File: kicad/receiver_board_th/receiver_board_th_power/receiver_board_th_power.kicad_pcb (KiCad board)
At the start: 2 copper layers, 31 x 63 mm, 12 parts, among them J1 B2B 1, J2 B2B 2, J3 Motor 1, J4 Motor 2, J5 Battery Mon, U1 ESP32-C3-SuperMini, U2 Dual H Bridge

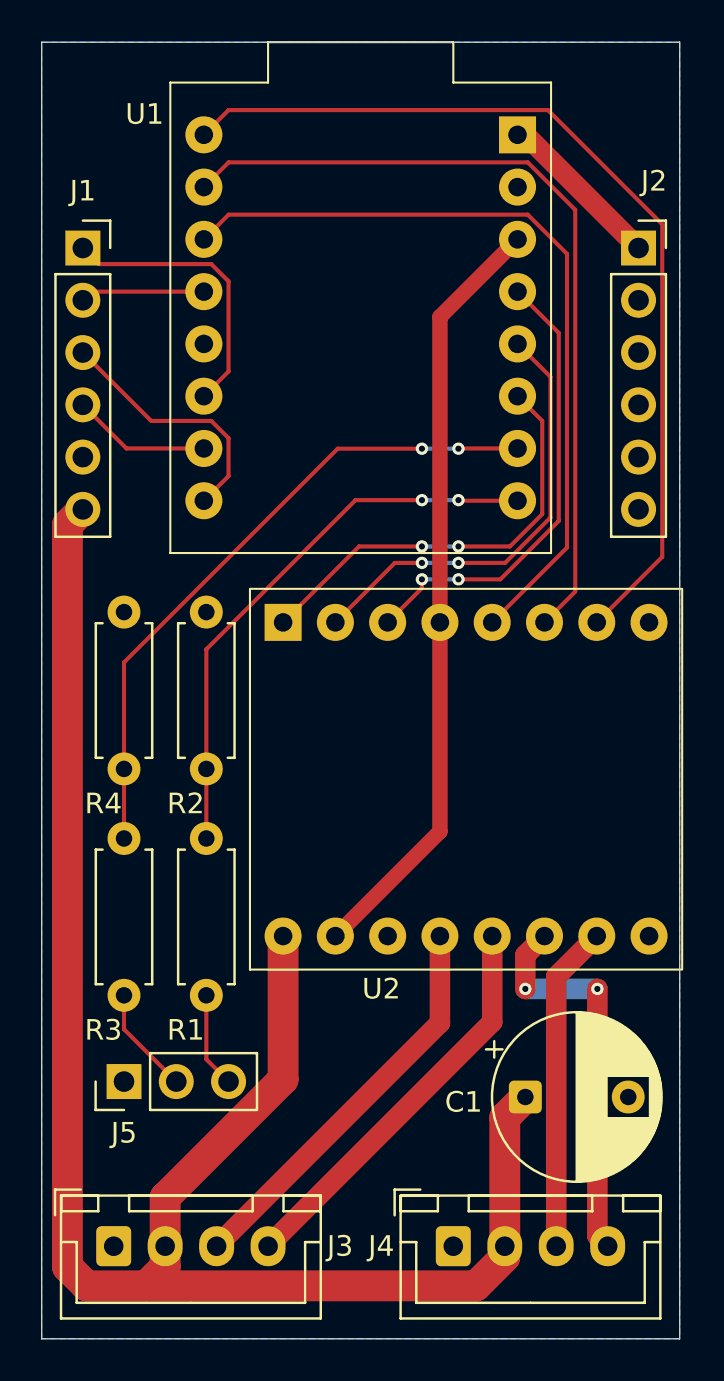
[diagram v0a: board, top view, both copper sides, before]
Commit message: Add M2 mounting holes to receiver power board
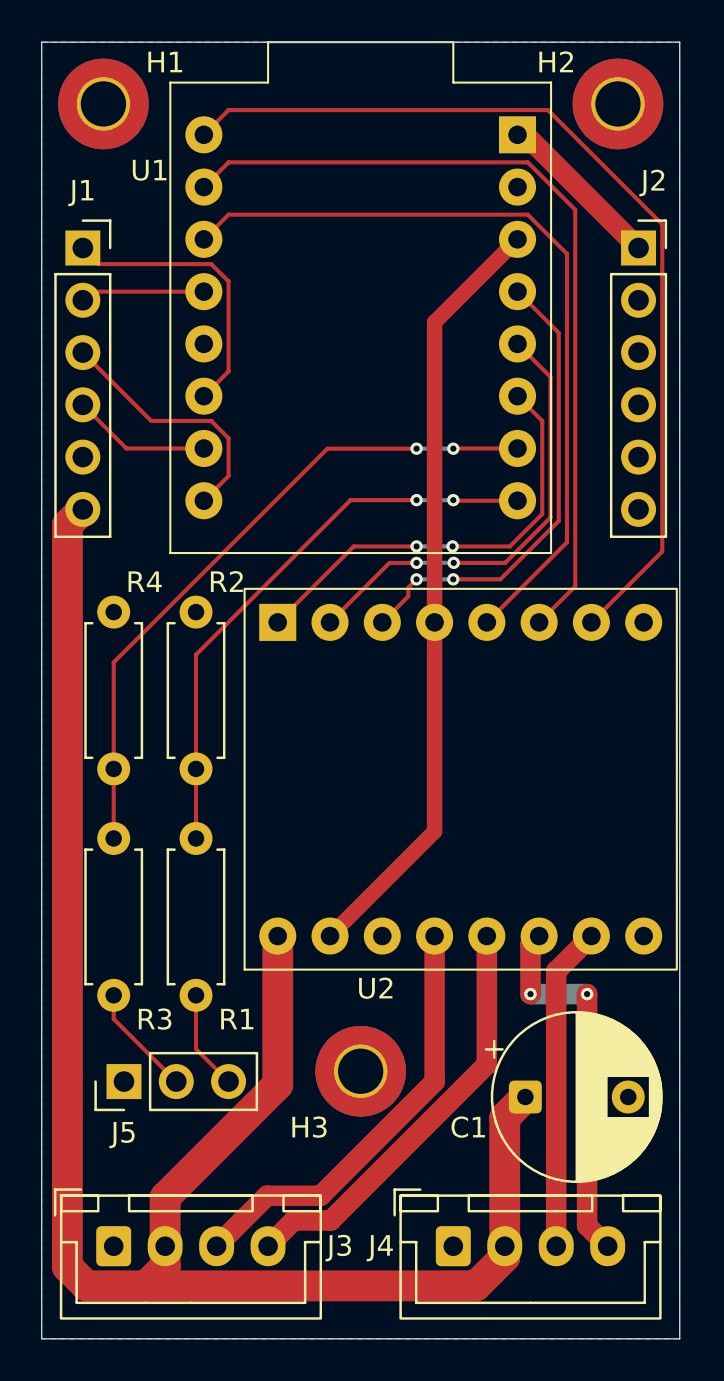
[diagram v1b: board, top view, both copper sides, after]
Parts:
- added H1: MountingHole, MountingHole:MountingHole_2.2mm_M2_Pad_TopBottom, F.Cu at (103.0, 103.0)
- added H2: MountingHole, MountingHole:MountingHole_2.2mm_M2_Pad_TopBottom, F.Cu at (128.0, 103.0)
- added H3: MountingHole, MountingHole:MountingHole_2.2mm_M2_Pad_TopBottom, F.Cu at (115.5, 150.0)
- moved R1 0.50 mm to (107.5, 146.3)
- moved R2 0.50 mm to (107.5, 135.3)
- moved R3 0.50 mm to (103.5, 146.3)
- moved R4 0.50 mm to (103.5, 135.3)
- moved U2 0.26 mm to (120.4, 135.8)
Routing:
- net /MOT1_C1: track 19.6 -> 21.0 mm
- net /MOT1_C2: track 19.6 -> 20.5 mm
- net /MOT2_C2: track 19.2 -> 18.4 mm
